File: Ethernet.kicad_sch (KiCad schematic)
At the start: 8 parts, among them J9 RJ45_LINK-PP_LPJG0926HENL_Hor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, U12 TPD4EUSB30, U13 TPD4EUSB30

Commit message: [WIP] PCB commit
Signed-off-by: Dominik Sliwa <dominik@sliwa.io>
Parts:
- R20: footprint Resistor_SMD:R_0402_1005Metric -> Resistor_SMD:R_1206_3216Metric
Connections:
- net ETH.TD2+: now also U12.5 (D2-); no longer U12.4 (D2+)
- net ETH.TD2-: now also U12.4 (D2+); no longer U12.5 (D2-)
- net ETH.TD4+: now also U13.5 (D2-); no longer U13.4 (D2+)
- net ETH.TD4-: now also U13.4 (D2+); no longer U13.5 (D2-)
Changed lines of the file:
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@@
     (effects (font (size 1.27 1.27)) (justify left bottom))
   )
-  (label "ETH.TD2+" (at 107.95 59.69 180)
+  (label "ETH.TD2-" (at 107.95 59.69 180)
     (effects (font (size 1.27 1.27)) (justify right bottom))
   )
-  (label "ETH.TD2-" (at 107.95 64.77 180)
+  (label "ETH.TD2+" (at 107.95 64.77 180)
     (effects (font (size 1.27 1.27)) (justify right bottom))
   )
-  (label "ETH.TD4+" (at 107.95 92.71 180)
+  (label "ETH.TD4-" (at 107.95 92.71 180)
     (effects (font (size 1.27 1.27)) (justify right bottom))
   )
-  (label "ETH.TD4-" (at 107.95 97.79 180)
+  (label "ETH.TD4+" (at 107.95 97.79 180)
     (effects (font (size 1.27 1.27)) (justify right bottom))
   )
@@
     (property "Reference" "R20" (id 0) (at 181.7432 133.35 0))
     (property "Value" "0R" (id 1) (at 190.392 135.89 0))
-    (property "Footprint" "Resistor_SMD:R_0402_1005Metric" (id 2) (at 184.15 135.89 0)
+    (property "Footprint" "Resistor_SMD:R_1206_3216Metric" (id 2) (at 184.15 135.89 0)
       (effects (font (size 1.27 1.27)) hide)
     )

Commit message: Change TPD4EUSB30 symbol for pass-through routing
Make the pads next to each input pad a passive connection as well to
allow pass-through routing.

Signed-off-by: Stefan Agner <stefan@agner.ch>
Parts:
- U12, U13: symbol Power_Protection:TPD4EUSB30 -> LightBlue:TPD4EUSB30
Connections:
- net ETH.TD1+: now also U12.10 (D1+)
- net ETH.TD1-: now also U12.9 (D1-)
- net ETH.TD2+: now also U12.6 (D2-)
- net ETH.TD2-: now also U12.7 (D2+)
- net ETH.TD3+: now also U13.10 (D1+)
- net ETH.TD3-: now also U13.9 (D1-)
- net ETH.TD4+: now also U13.6 (D2-)
- net ETH.TD4-: now also U13.7 (D2+)
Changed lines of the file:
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@@
     (comment 2 "Light Blue")
   )
+  (bus_alias "ETH" (members "TD1+" "TD1-" "TD2+" "TD2-" "TD3+" "TD3-" "TD4+" "TD4-" "LED_YELLOW" "LED_GREEN"))
   (bus_alias "PoE" (members "VC1" "VC2" "VC3" "VC4"))
-  (bus_alias "ETH" (members "TD1+" "TD1-" "TD2+" "TD2-" "TD3+" "TD3-" "TD4+" "TD4-" "LED_YELLOW" "LED_GREEN"))
   (junction (at 153.67 80.01) (diameter 0.9144) (color 0 0 0 0))
   (junction (at 177.8 130.81) (diameter 0.9144) (color 0 0 0 0))
@@
     (property "Config" "DNP" (id 4) (at 166.37 138.43 0))
   )
-  (symbol (lib_id "Power_Protection:TPD4EUSB30") (at 85.09 62.23 0) (unit 1)
+  (symbol (lib_name "Power_Protection:TPD4EUSB30_1") (lib_id "LightBlue:TPD4EUSB30") (at 85.09 62.23 0) (unit 1)
     (in_bom yes) (on_board yes)
     (property "Reference" "U12" (id 0) (at 85.09 49.53 0))
@@
     )
   )
-  (symbol (lib_id "Power_Protection:TPD4EUSB30") (at 85.09 95.25 0) (unit 1)
+  (symbol (lib_id "LightBlue:TPD4EUSB30") (at 85.09 95.25 0) (unit 1)
     (in_bom yes) (on_board yes)
     (property "Reference" "U13" (id 0) (at 85.09 82.55 0))

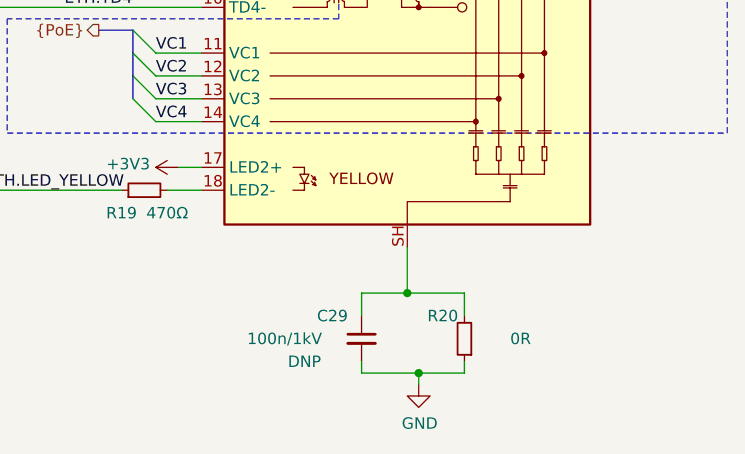
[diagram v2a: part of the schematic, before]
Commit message: PCB[WIP]: finished routing
TODO
- length matching
- review
- silkscreen

Signed-off-by: Dominik Sliwa <dominik@sliwa.io>
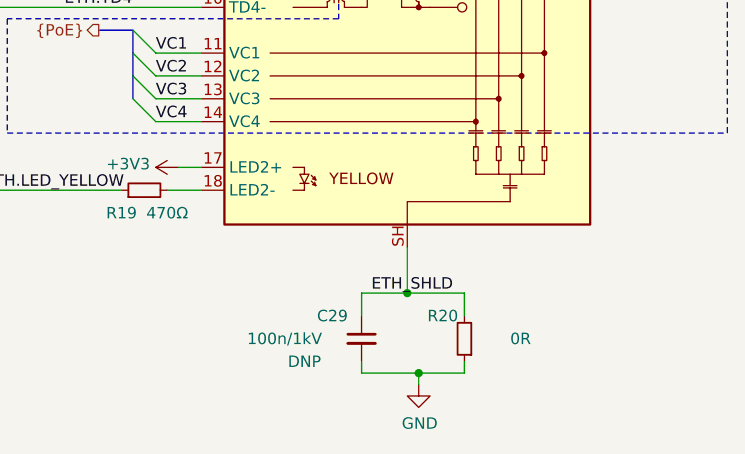
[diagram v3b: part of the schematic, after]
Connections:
- net ETH_SHLD: now reaches C29.1, J9.SH, R20.2
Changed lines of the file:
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@@
     (effects (font (size 1.27 1.27)) (justify left bottom))
+  )
+  (label "ETH_SHLD" (at 182.88 130.81 180)
+    (effects (font (size 1.27 1.27)) (justify right bottom))
   )
   (hierarchical_label "ETH{ETH}" (shape bidirectional) (at 124.46 53.34 180)

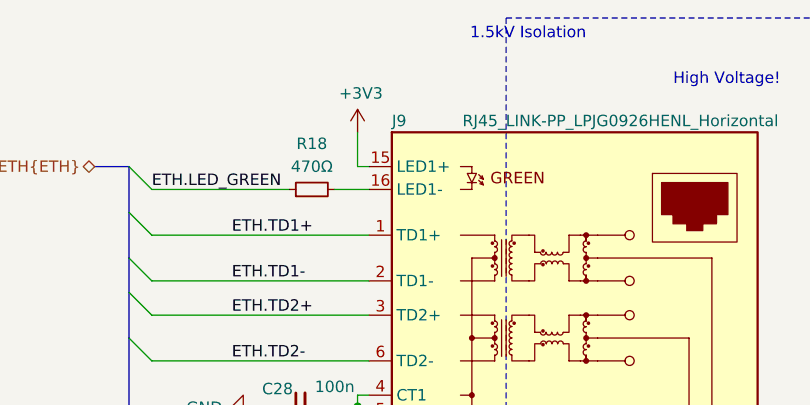
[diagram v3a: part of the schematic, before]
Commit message: Improve SW and D (LED) ordering and silkscreen
Make sure switches (SW) are ordered logically. Also use D1 through D6
for LEDs.

Signed-off-by: Stefan Agner <stefan@agner.ch>
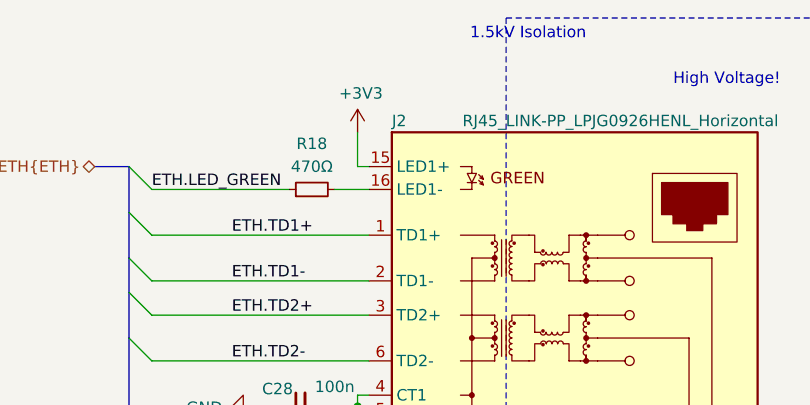
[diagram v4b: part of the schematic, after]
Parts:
- renumbered J9 to J2
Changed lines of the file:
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@@
     (comment 2 "Light Blue")
   )
+  (bus_alias "PoE" (members "VC1" "VC2" "VC3" "VC4"))
   (bus_alias "ETH" (members "TD1+" "TD1-" "TD2+" "TD2-" "TD3+" "TD3-" "TD4+" "TD4-" "LED_YELLOW" "LED_GREEN"))
-  (bus_alias "PoE" (members "VC1" "VC2" "VC3" "VC4"))
   (junction (at 153.67 80.01) (diameter 0.9144) (color 0 0 0 0))
   (junction (at 177.8 130.81) (diameter 0.9144) (color 0 0 0 0))
@@
   (symbol (lib_id "LightBlue:RJ45_LINK-PP_LPJG0926HENL_Horizontal") (at 177.8 86.36 0) (unit 1)
     (in_bom yes) (on_board yes)
-    (property "Reference" "J9" (id 0) (at 157.48 48.26 0)
+    (property "Reference" "J2" (id 0) (at 157.48 48.26 0)
       (effects (font (size 1.27 1.27)) (justify left))
     )

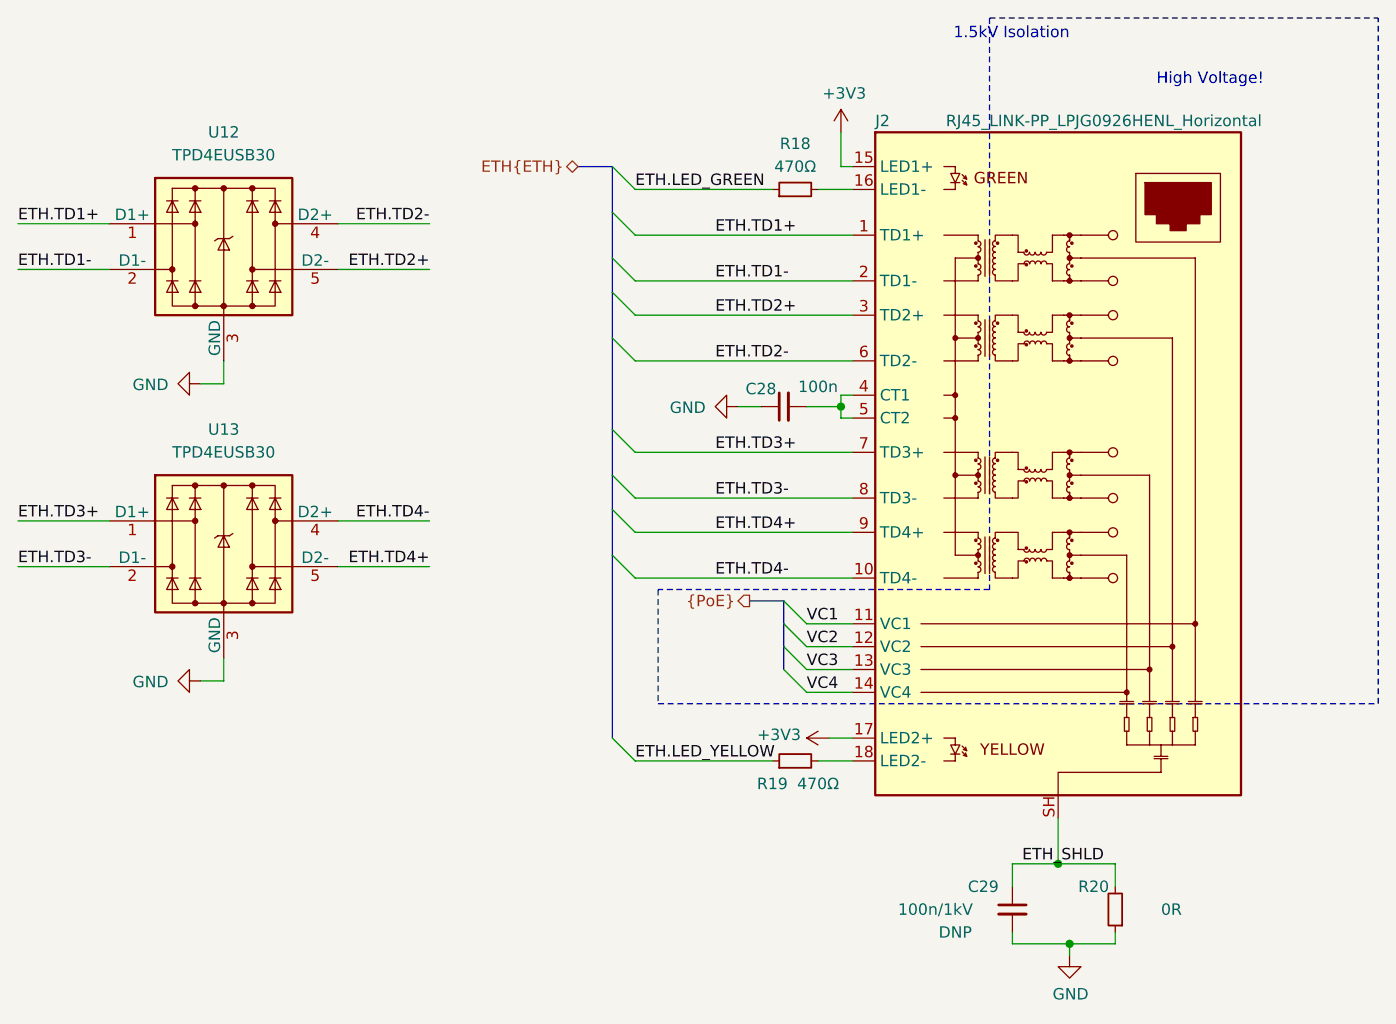
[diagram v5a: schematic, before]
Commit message: Replace Ohm sign with R
Adhere to our KiCad Style Guide and use R instead of the Ohm sign.

Signed-off-by: Stefan Agner <stefan@agner.ch>
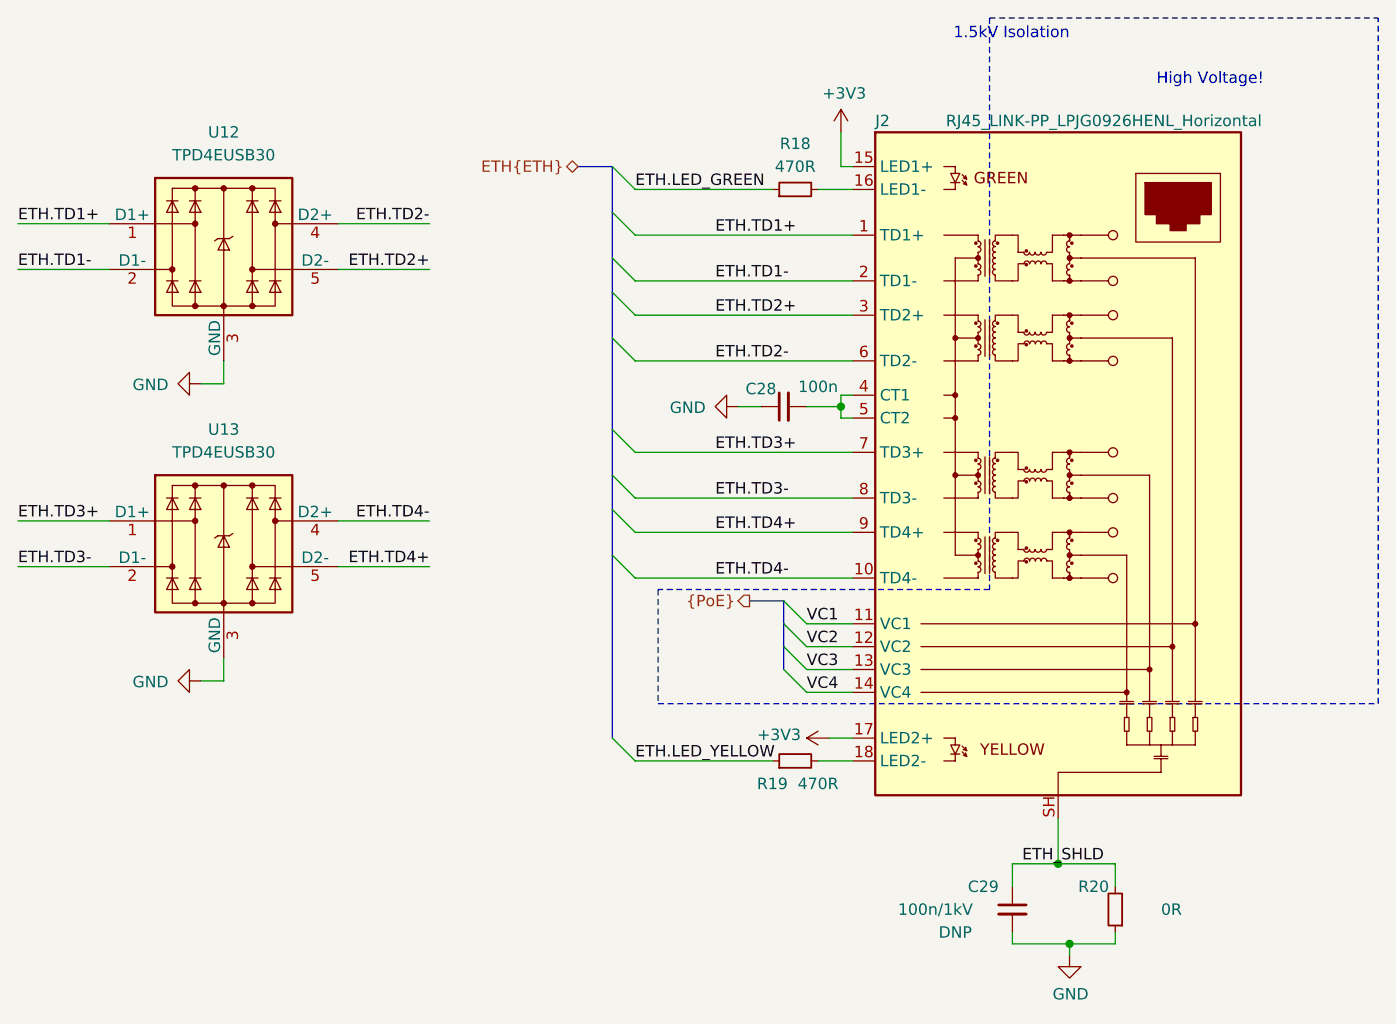
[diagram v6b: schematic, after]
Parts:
- R18, R19: value 470Ω -> 470R
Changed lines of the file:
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@@
     (in_bom yes) (on_board yes)
     (property "Reference" "R18" (id 0) (at 148.59 50.8 90))
-    (property "Value" "470Ω" (id 1) (at 148.59 53.34 90))
+    (property "Value" "470R" (id 1) (at 148.59 53.34 90))
     (property "Footprint" "Resistor_SMD:R_0402_1005Metric" (id 2) (at 148.59 55.88 0)
       (effects (font (size 1.27 1.27)) hide)
@@
     (in_bom yes) (on_board yes)
     (property "Reference" "R19" (id 0) (at 146.05 121.92 90))
-    (property "Value" "470Ω" (id 1) (at 151.13 121.92 90))
+    (property "Value" "470R" (id 1) (at 151.13 121.92 90))
     (property "Footprint" "Resistor_SMD:R_0402_1005Metric" (id 2) (at 148.59 119.38 0)
       (effects (font (size 1.27 1.27)) hide)

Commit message: Assign footprints and annotate components
Signed-off-by: Stefan Agner <stefan@agner.ch>
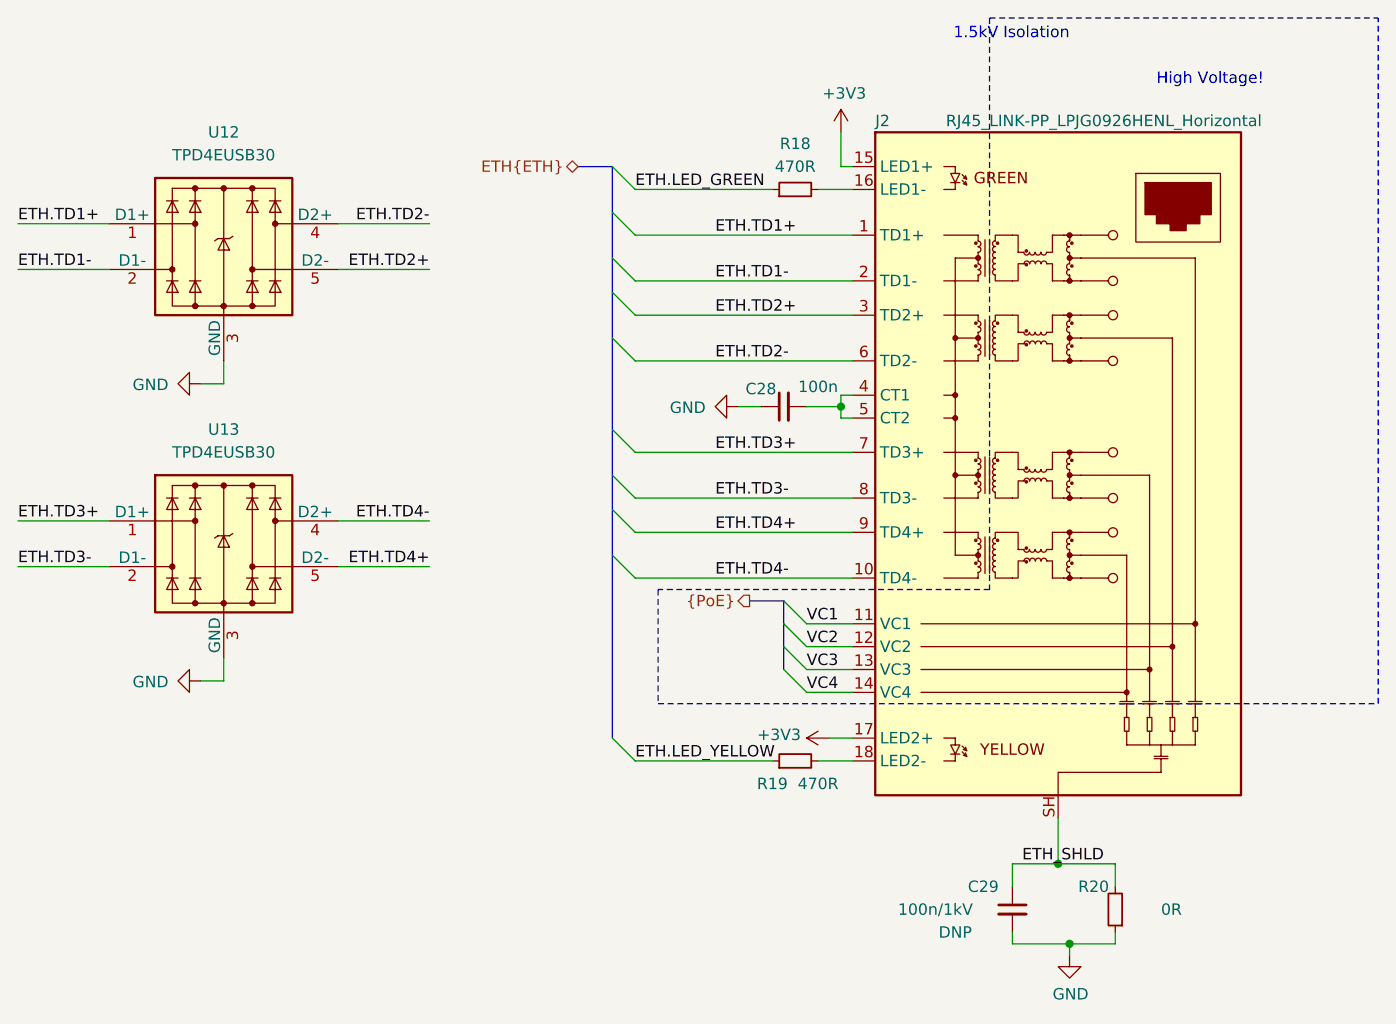
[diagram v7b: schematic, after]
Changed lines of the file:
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@@
-(kicad_sch (version 20210126) (generator eeschema)
+(kicad_sch (version 20210406) (generator eeschema)
   (paper "A4")
   (title_block
@@
     (comment 2 "Light Blue")
   )
+  (bus_alias "PoE" (members "VC1" "VC2" "VC3" "VC4"))
   (bus_alias "ETH" (members "TD1+" "TD1-" "TD2+" "TD2-" "TD3+" "TD3-" "TD4+" "TD4-" "LED_YELLOW" "LED_GREEN"))
-  (bus_alias "PoE" (members "VC1" "VC2" "VC3" "VC4"))
   (junction (at 153.67 80.01) (diameter 0.9144) (color 0 0 0 0))
   (junction (at 177.8 130.81) (diameter 0.9144) (color 0 0 0 0))
@@
     (stroke (width 0) (type solid) (color 0 0 0 0))
   )
-  (bus (pts (xy 128.27 53.34) (xy 128.27 58.42))
-    (stroke (width 0) (type solid) (color 0 0 0 0))
-  )
-  (bus (pts (xy 128.27 58.42) (xy 128.27 63.5))
-    (stroke (width 0) (type solid) (color 0 0 0 0))
-  )
-  (bus (pts (xy 128.27 63.5) (xy 128.27 67.31))
-    (stroke (width 0) (type solid) (color 0 0 0 0))
-  )
-  (bus (pts (xy 128.27 67.31) (xy 128.27 72.39))
-    (stroke (width 0) (type solid) (color 0 0 0 0))
-  )
-  (bus (pts (xy 128.27 72.39) (xy 128.27 82.55))
-    (stroke (width 0) (type solid) (color 0 0 0 0))
-  )
-  (bus (pts (xy 128.27 82.55) (xy 128.27 87.63))
-    (stroke (width 0) (type solid) (color 0 0 0 0))
-  )
-  (bus (pts (xy 128.27 87.63) (xy 128.27 91.44))
-    (stroke (width 0) (type solid) (color 0 0 0 0))
-  )
-  (bus (pts (xy 128.27 91.44) (xy 128.27 96.52))
-    (stroke (width 0) (type solid) (color 0 0 0 0))
-  )
-  (bus (pts (xy 128.27 96.52) (xy 128.27 116.84))
+  (bus (pts (xy 128.27 53.34) (xy 128.27 116.84))
     (stroke (width 0) (type solid) (color 0 0 0 0))
   )
@@
     (stroke (width 0) (type solid) (color 0 0 0 0))
   )
-  (bus (pts (xy 147.32 101.6) (xy 147.32 104.14))
-    (stroke (width 0) (type solid) (color 0 0 0 0))
-  )
-  (bus (pts (xy 147.32 104.14) (xy 147.32 106.68))
-    (stroke (width 0) (type solid) (color 0 0 0 0))
-  )
-  (bus (pts (xy 147.32 106.68) (xy 147.32 109.22))
+  (bus (pts (xy 147.32 101.6) (xy 147.32 109.22))
     (stroke (width 0) (type solid) (color 0 0 0 0))
   )
@@
     )
     (pin "1")
+    (pin "10")
     (pin "2")
     (pin "3")
     (pin "4")
     (pin "5")
+    (pin "6")
+    (pin "7")
     (pin "8")
-    (pin "10")
-    (pin "7")
-    (pin "6")
     (pin "9")
   )
@@
     )
     (pin "1")
+    (pin "10")
     (pin "2")
     (pin "3")
     (pin "4")
     (pin "5")
+    (pin "6")
+    (pin "7")
     (pin "8")
-    (pin "10")
-    (pin "7")
-    (pin "6")
     (pin "9")
   )
@@
       (effects (font (size 1.27 1.27)) hide)
     )
-    (pin "4")
-    (pin "2")
-    (pin "1")
-    (pin "18")
-    (pin "17")
-    (pin "16")
-    (pin "15")
-    (pin "8")
-    (pin "7")
-    (pin "3")
-    (pin "6")
-    (pin "5")
-    (pin "9")
+    (pin "1")
     (pin "10")
-    (pin "SH")
     (pin "11")
     (pin "12")
     (pin "13")
     (pin "14")
+    (pin "15")
+    (pin "16")
+    (pin "17")
+    (pin "18")
+    (pin "2")
+    (pin "3")
+    (pin "4")
+    (pin "5")
+    (pin "6")
+    (pin "7")
+    (pin "8")
+    (pin "9")
+    (pin "SH")
   )
 )
